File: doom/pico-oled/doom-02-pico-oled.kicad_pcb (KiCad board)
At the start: 2 copper layers, 150 x 100 mm, 43 parts, among them Q1 AO3401A, Q2 FS8205A, SW1 PTS645SM43SMTR92 LFS, SW2 PTS645SM43SMTR92 LFS, SW3 PTS645SM43SMTR92 LFS, SW4 PTS645SM43SMTR92 LFS, SW5 PTS645SM43SMTR92 LFS, SW6 PTS645SM43SMTR92 LFS, SW7 PTS645SM43SMTR92 LFS, SW8 PTS645SM43SMTR92 LFS, SW9 MSK12C02, U1 SC0915, U2 DW01A, U3 BQ24075RGTR

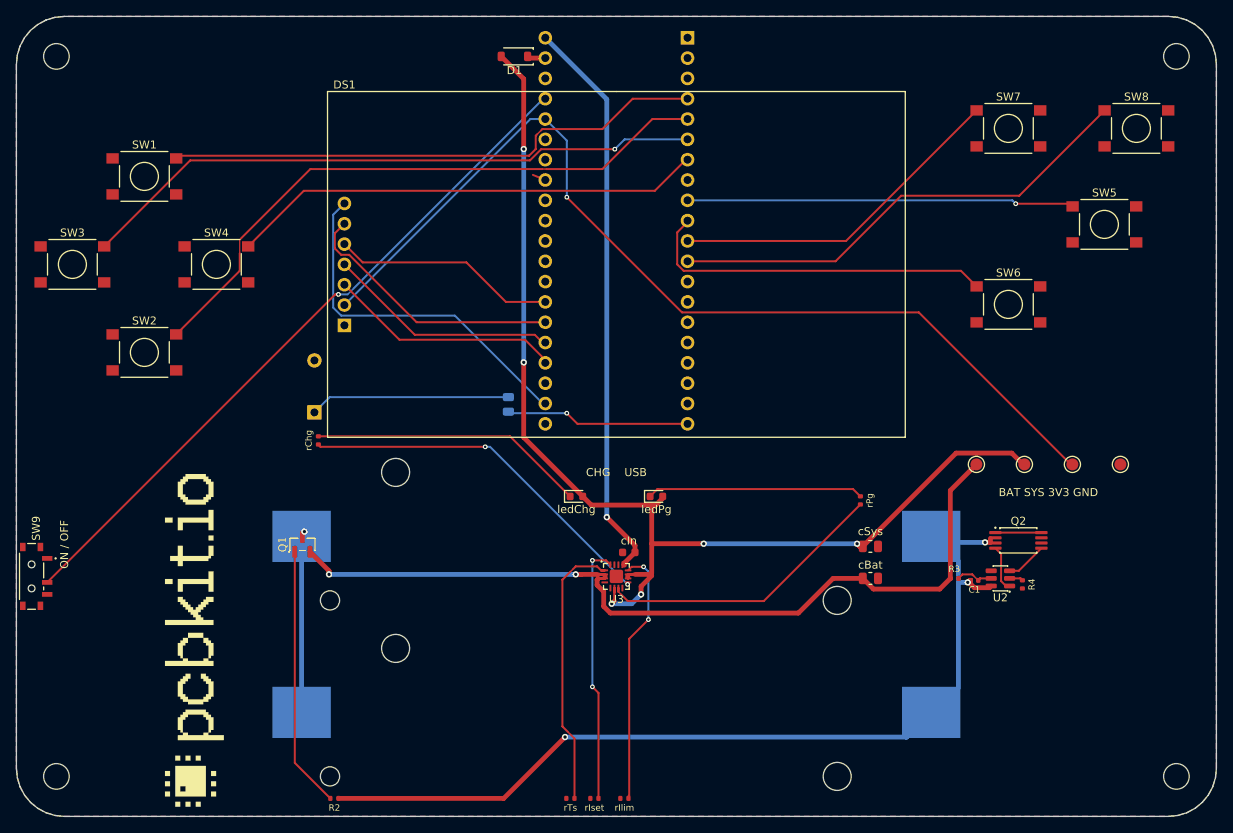
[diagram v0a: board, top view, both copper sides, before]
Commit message: Boards pass check and KiCad 10's DRC again: holes in courtyards, the USB net rename
pcbkit's check now has KiCad 10's pth/npth_inside_courtyard (pcbkit be5b6955), and 13 boards
failed it. KiCad's own DRC (kicad-cli 10) reports the same holes on every one of them.

- Parts that really stand above the holes under them (a screen or a Nano on its sockets, the
  Delta-S02's КМ-6 capacitors flat under its chips, as the factory placed them): a courtyard rule
  for the pair, written to each board's .kicad_dru, so KiCad's DRC agrees.
- Real collisions moved: servo-controller's dial 3 mm up (the Nano's socket pins came out under
  it), c3-pocket's fourth M3 hole from under a cell holder to the top edge's middle, s3-rgb's
  D-pad 2 mm up (a holder's peg came through under the down key).
- v003-emu, c3-pocket, rp2040-tft, rp2350-psram, s3-rgb, teensy41: re-routed for the standard USB
  block's renamed net (usb/raw is usb/vbusIn since pcbkit 2088839e): their tracks still carried
  the old name and shorted the fuse and connector pads.
- p4-touch-7: its board file still had a courtyard for the panel the design gives none (KiCad
  reported 114 courtyard errors); written again.

Measured on the dev host: all 44 registry boards `pcbkit check` complete with 0 errors, and
kicad-cli pcb drc 0 errors on every board.

Claude-Session: https://claude.ai/code/session_018URVYF1YPgyrMNetY9yT1T
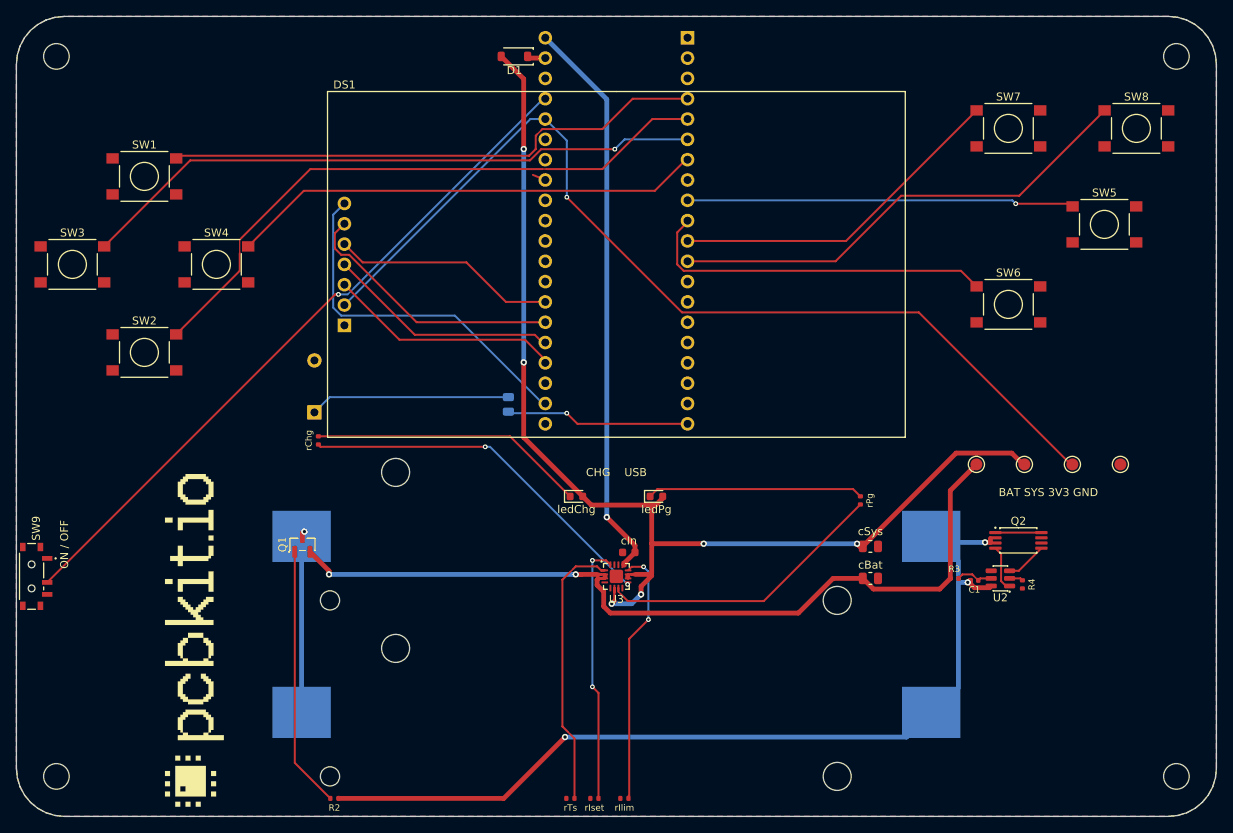
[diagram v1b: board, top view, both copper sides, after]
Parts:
- H1, H2, H3, H4: value (none) -> MountingHole_3.2mm_M3
- logo: value (none) -> Logo_PCBKit_pcbkit.io
- tpBat, tpGnd, tpSys, tpV3: value (none) -> TestPoint_Round_D1.5mm
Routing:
- net CELL_N: track 121.3 -> 108.0 mm
- net SYS: track 150.7 -> 146.0 mm
- net BAT: track 108.6 -> 106.5 mm
- net FIRE: track 49.4 -> 48.4 mm
- net UP: track 68.9 -> 68.0 mm
- net Net-(C1-1): track 5.42 -> 4.72 mm
- net Net-(R4-1): track 2.38 -> 1.70 mm
- net VSYS: track 2.89 -> 2.30 mm

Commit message: doom: a resettable fuse per 18650 cell, a 2 % backlight clamp, a 1 A LDO on the S3 boards
The verifier (wiring-parallel-cells) found the two holders of every Doom board directly in parallel:
a cell put in backwards, or one much fuller than the other, drives the other through nothing but
the cells' resistance (about 56-168 A). Each holder's + now reaches BAT_IN through its own 2 A
resettable fuse (Littelfuse 1812L200/16GR, C18198340: 16 V, 100 A interrupting) on new nets
CELL1_P / CELL2_P. Nothing else moved; the boards were re-routed for the new nets.

- s3-rgb: the MT3608 backlight's open-panel clamp was a 28 V 5 % zener (bound 30.0 V against the
  switch's 30 V). It is now two 2 % zeners in series, UDZVTE-1718B + UDZVTE-1710B (27.33-28.56 V;
  LCSC stocks no single 28 V 2 % part). That is under 29.2 V and above the panel's 27.2 V.
- s3-rgb, s3-handheld: TLV75533 (500 mA) -> TLV75733 (1 A, C485517, same DBV pins; sheet from
  SBVS322C), for the ESP32-S3's 500 mA supply peaks (erc-supply-peak).
- c3-pocket, v003-emu: the USB PTC's hold is 750 mA, as the part (nSMD075) is (rating-current).
- pico2-carrier: the CHG/PG LEDs 1.5 mm further from the display's courtyard. rp2350-handheld:
  the logo off the LCD's courtyard and BT1's peg.
- READMEs: the per-cell fuses, the boards already ordered (s3-rgb, JLC W2026102705013253: insert
  the cells one at a time), status and BOM as check and the fab export give them now.

Measured on the dev host (pcbkit 5e0d2cc8): all 11 complete, 0 errors, 0 unrouted. What is left is
erc-rail-name (sent to the verifier as false positives) and full-speed USB pair coupling. The MCU
pins' nets are unchanged on every board, so the firmware and its simulation are unchanged.

Claude-Session: https://claude.ai/code/session_01B3VRfBCg9vAvGVWujVGarr
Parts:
- added F1: PTC 2000mA, Fuse_1812_4532Metric, B.Cu at (128.5, 179.8)
- added F2: PTC 2000mA, Fuse_1812_4532Metric, B.Cu at (129.8, 170.2)
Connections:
- BT1 pad 2: BAT_IN -> CELL1_P
- BT2 pad 2: BAT_IN -> CELL2_P
- SW1 pad 2: UP -> GND
- SW2 pad 2: DOWN -> GND
- SW3 pad 2: LEFT -> GND
- SW4 pad 2: RIGHT -> GND
- SW5 pad 2: FIRE -> GND
- SW6 pad 2: USE -> GND
- SW7 pad 2: STRAFE -> GND
- SW8 pad 2: MENU -> GND
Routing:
- net CELL1_P: track 0.00 -> 9.27 mm
- net CELL2_P: track 0.00 -> 7.19 mm
- net BAT_IN: track 22.0 -> 17.0 mm
